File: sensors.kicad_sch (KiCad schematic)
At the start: 69 parts, among them J1 1-4, J2 5-8, U1 ADG707, U2 OPA2340, U3 OPA2340

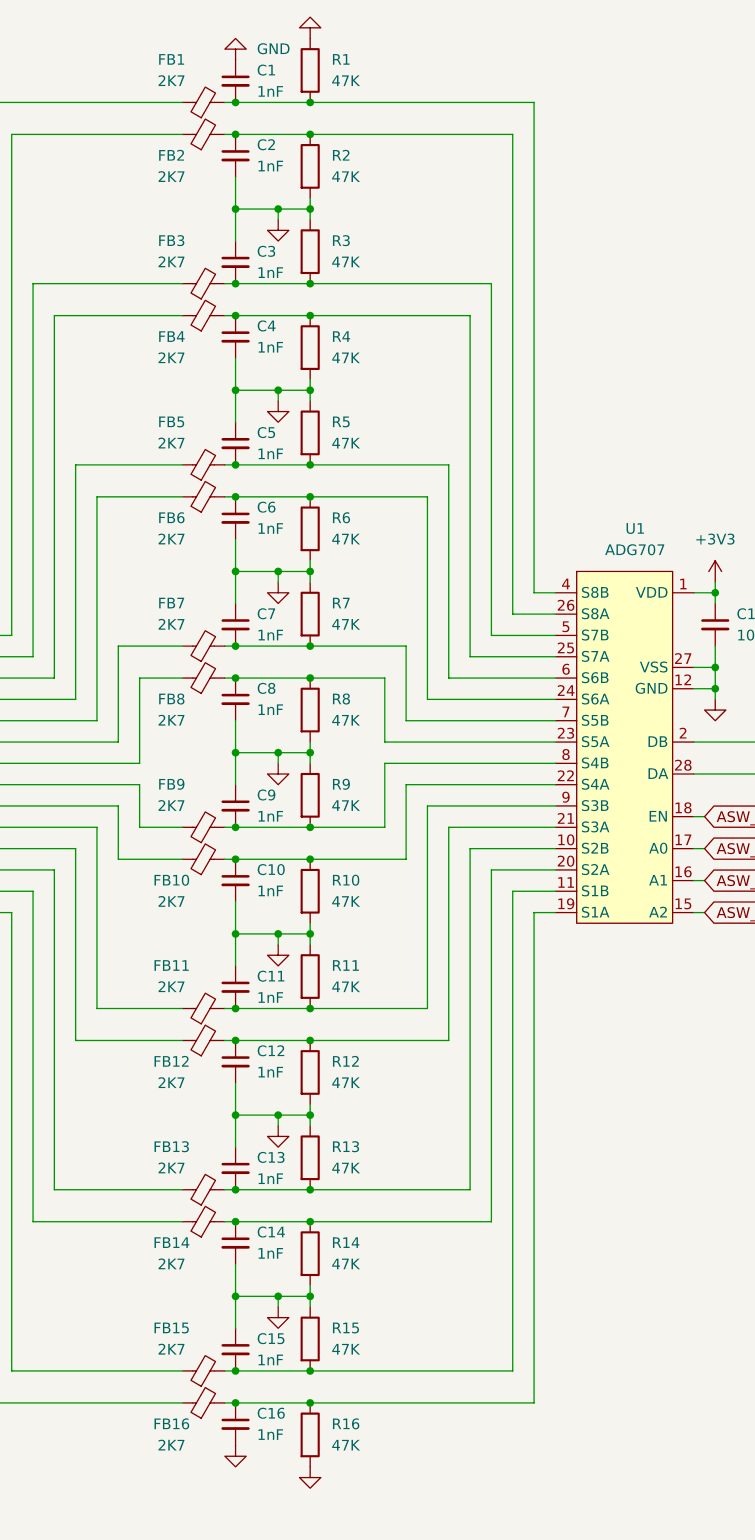
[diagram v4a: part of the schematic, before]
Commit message: replace sensor wire esd caps with TVSs
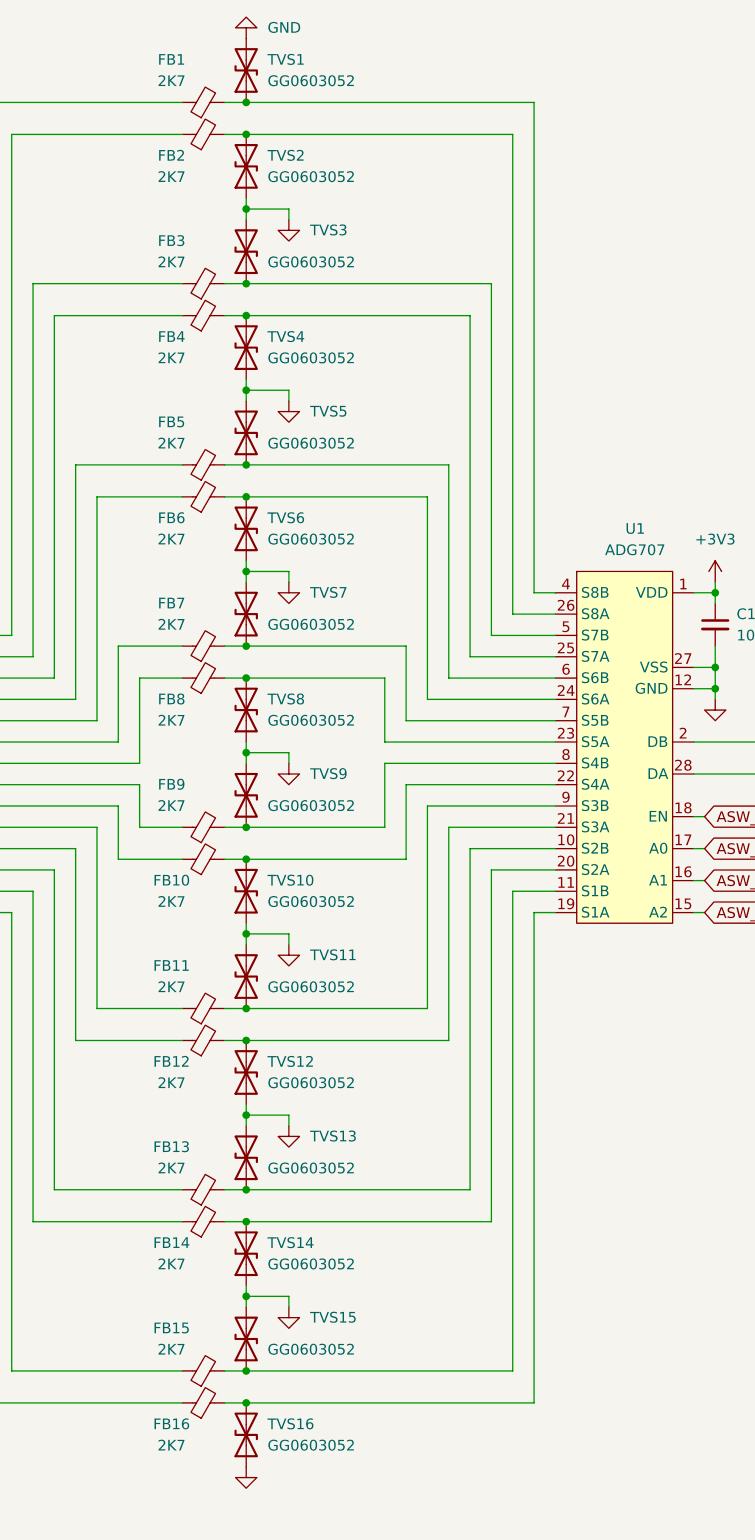
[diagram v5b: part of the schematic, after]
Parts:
- removed C1, C10, C11, C12, C13, C14, C15, C16, C2, C3, C4, C5, C6, C7, C8, C9: 1nF, Capacitor_SMD:C_0603_1608Metric_Pad1.08x0.95mm_HandSolder, symbol Device:C_Small
- removed R1, R10, R11, R12, R13, R14, R15, R16, R2, R3, R4, R5, R6, R7, R8, R9: 47K, Resistor_SMD:R_0603_1608Metric_Pad0.98x0.95mm_HandSolder, symbol Device:R
- added TVS1, TVS10, TVS11, TVS12, TVS13, TVS14, TVS15, TVS16, TVS2, TVS3, TVS4, TVS5, TVS6, TVS7, TVS8, TVS9: GG0603052, Diode_SMD:D_0603_1608Metric_Pad1.05x0.95mm_HandSolder, symbol Device:D_TVS
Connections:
- net GND: now also TVS1.2 (A2), TVS10.1 (A1), TVS11.2 (A2), TVS12.1 (A1), TVS13.2 (A2), TVS14.1 (A1), TVS15.2 (A2), TVS16.1 (A1), TVS2.1 (A1), TVS3.2 (A2), TVS4.1 (A1), TVS5.2 (A2), TVS6.1 (A1), TVS7.2 (A2), TVS8.1 (A1), TVS9.2 (A2)
- net at FB8.2, U1.23 (S5A): now also TVS8.2 (A2)
- net at FB16.2, U1.19 (S1A): now also TVS16.2 (A2)
- net at FB11.2, U1.9 (S3B): now also TVS11.1 (A1)
- net at FB2.2, U1.26 (S8A): now also TVS2.2 (A2)
- net at FB1.2, U1.4 (S8B): now also TVS1.1 (A1)
- net at FB7.2, U1.7 (S5B): now also TVS7.1 (A1)
- net at FB15.2, U1.11 (S1B): now also TVS15.1 (A1)
- net at FB14.2, U1.20 (S2A): now also TVS14.2 (A2)
- net at FB4.2, U1.25 (S7A): now also TVS4.2 (A2)
- net at FB3.2, U1.5 (S7B): now also TVS3.1 (A1)
- net at FB12.2, U1.21 (S3A): now also TVS12.2 (A2)
- net at FB10.2, U1.22 (S4A): now also TVS10.2 (A2)
- net at FB6.2, U1.24 (S6A): now also TVS6.2 (A2)
- net at FB5.2, U1.6 (S6B): now also TVS5.1 (A1)
- net at FB13.2, U1.10 (S2B): now also TVS13.1 (A1)
- net at FB9.2, U1.8 (S4B): now also TVS9.1 (A1)

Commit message: generate gerbers
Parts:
- removed C18: 100nF, Capacitor_SMD:C_0603_1608Metric_Pad1.08x0.95mm_HandSolder, symbol Device:C_Small
- removed U2: OPA2340, Package_SO:SOP-8_3.9x4.9mm_P1.27mm, symbol Amplifier_Operational:OPA2340
- added C1, C2: 10pF, Capacitor_SMD:C_0603_1608Metric_Pad1.08x0.95mm_HandSolder, symbol Device:C_Small
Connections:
- net at C39.2: now also R18.2, U1.28 (DA)
- net at R19.2, R21.2, U3.3 (+): now also C1.2
- net at R20.2, R22.1, U3.2 (-): now also C2.2
- net at R22.2, U3.1, U3.6 (-): now also C2.1
- net at R21.1, R25.2, R26.1: now also C1.1
- net at R17.2, U1.2 (DB): now also C20.2
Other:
- moved on the sheet: C19, C20, C39, R19, R20, R21, R22, R23, R24, R25, R26, R45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

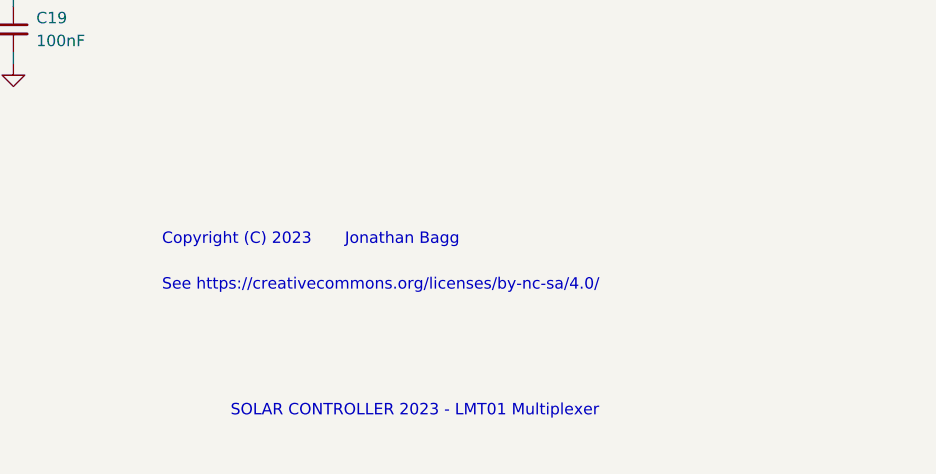
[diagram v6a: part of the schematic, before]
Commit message: add github link to title block and print schematic pdf
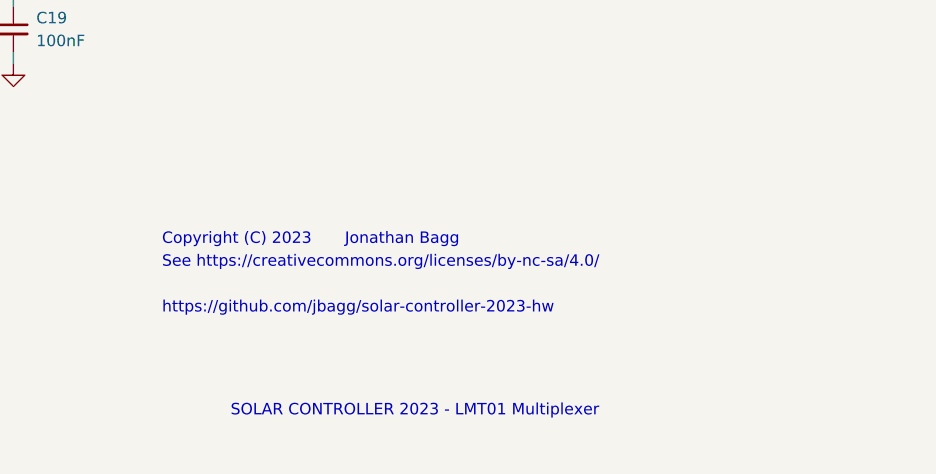
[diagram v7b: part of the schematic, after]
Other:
- note added: "https://github.com/jbagg/solar-controller-2023-hw"
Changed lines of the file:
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@@
   )
   (text "See https://creativecommons.org/licenses/by-nc-sa/4.0/"
-    (at 180.34 176.53 0)
+    (at 180.34 173.99 0)
     (effects (font (size 1.27 1.27)) (justify left bottom))
   )
+  (text "https://github.com/jbagg/solar-controller-2023-hw" (at 180.34 179.07 0)
+    (effects (font (size 1.27 1.27)) (justify left bottom))
+  )
